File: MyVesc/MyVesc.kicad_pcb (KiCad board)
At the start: 4 copper layers, 100 x 70 mm, 112 parts, among them J1 CAN, J10 GATE_PH_A, J11 CURR_SENS_PH_A, J12 CURR_SENS_PH_B, J13 CURR_SENS_PH_C, J14 Pull_up, J2 Conn_01x08, J4 Conn_01x03, J5 UNUSED MCU PINS, J6 TEMP_SENS, J7 V_IN, J8 GATE_PH_C, J9 GATE_PH_B, P4 HALL/Encoder, P5 SWD, U1 TJA1051T/3/1J, U10 LM5161, U11 MCP16311/2, U12 MCP16311/2, U13 INA240, U14 INA240, U15 INA240, U2 BMI160, U3 STM32F405RGT6, U4 UCC2721x, U5 UCC2721x, U6 UCC2721x, Y1 8M

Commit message: routerd logic board
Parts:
- removed C61, C62: 2.2u, Capacitor_SMD:C_0603_1608Metric
- removed J10: GATE_PH_A, Connector_PinHeader_1.00mm:PinHeader_1x06_P1.00mm_Vertical
- removed J11: CURR_SENS_PH_A, Connector_PinHeader_1.00mm:PinHeader_1x04_P1.00mm_Vertical
- removed J12: CURR_SENS_PH_B, Connector_PinHeader_1.00mm:PinHeader_1x04_P1.00mm_Vertical
- removed J13: CURR_SENS_PH_C, Connector_PinHeader_1.00mm:PinHeader_1x04_P1.00mm_Vertical
- removed J9: GATE_PH_B, Connector_PinHeader_1.00mm:PinHeader_1x06_P1.00mm_Vertical
- removed R1: 22R, Resistor_SMD:R_0603_1608Metric
- removed U13, U14, U15: INA240, Package_SO:SOIC-8_3.9x4.9mm_P1.27mm
- added C24: 2.2u, Capacitor_SMD:C_0603_1608Metric, F.Cu at (234.1, 123.8)
- added C25: 2.2u, Capacitor_SMD:C_0603_1608Metric, F.Cu at (243.0, 148.8)
- added C26: 2.2u, Capacitor_SMD:C_0603_1608Metric, F.Cu at (277.9, 145.7)
- added C48: 2.2u, Capacitor_SMD:C_0603_1608Metric, F.Cu at (263.4, 150.5)
- added C49: 2.2u, Capacitor_SMD:C_0603_1608Metric, F.Cu at (286.6, 147.2)
- added J15: PH_C_CONNECTOR, Connector_PinSocket_2.54mm:PinSocket_2x04_P2.54mm_Vertical, B.Cu at (297.3, 151.3)
- added J3: PH_A_CONNECTOR, Connector_PinSocket_2.54mm:PinSocket_2x04_P2.54mm_Vertical, B.Cu at (207.9, 151.6)
- added R30: 10k, Resistor_SMD:R_0603_1608Metric, F.Cu at (235.2, 122.7)
- added R31: 10k, Resistor_SMD:R_0603_1608Metric, F.Cu at (241.4, 148.8)
- added R32: 10k, Resistor_SMD:R_0603_1608Metric, F.Cu at (276.3, 145.7)
- added U7: INA210, Package_TO_SOT_SMD:SOT-363_SC-70-6, F.Cu at (215.6, 150.5)
- added U8: INA210, Package_TO_SOT_SMD:SOT-363_SC-70-6, F.Cu at (260.9, 150.5)
- added U9: INA210, Package_TO_SOT_SMD:SOT-363_SC-70-6, F.Cu at (286.6, 149.7)
- C13, R16, R17, R18, R2, R20, R21, R22, R3, R4, R5, R6: moved to F.Cu
- J6: value TEMP_SENS -> PH_B_CONNECTOR; footprint Connector_PinHeader_1.00mm:PinHeader_1x08_P1.00mm_Vertical -> Connector_PinSocket_2.54mm:PinSocket_2x04_P2.54mm_Vertical; moved to B.Cu
- J7: footprint Connector_PinHeader_1.00mm:PinHeader_1x02_P1.00mm_Vertical -> Connector_PinSocket_2.54mm:PinSocket_1x02_P2.54mm_Vertical; moved to B.Cu
- J8: value GATE_PH_C -> NRF bluetooth; footprint Connector_PinHeader_1.00mm:PinHeader_1x06_P1.00mm_Vertical -> Connector_JST:JST_PH_B4B-PH-K_1x04_P2.00mm_Vertical
- USB1: footprint Connector_USB:USB_Micro-B_Wuerth_614105150721_Vertical -> Connector_USB:USB_Mini-B_Lumberg_2486_01_Horizontal
- moved J4 281.9 mm to (282.4, 89.0), turned to 180 degrees
- moved C1 276.7 mm to (282.4, 93.2), turned to -90 degrees
- moved R10 270.3 mm to (278.4, 93.2), turned to 90 degrees
- moved P4 260.0 mm to (297.6, 97.4), turned to -90 degrees
- moved J14 253.7 mm to (292.1, 107.0)
- moved R4 251.9 mm to (294.5, 104.2), turned to 90 degrees
- moved R5 251.7 mm to (292.9, 104.2), turned to 90 degrees
- moved R6 251.7 mm to (291.4, 104.2), turned to 90 degrees
- moved J6 239.9 mm to (252.8, 151.6)
- moved R2 216.2 mm to (290.8, 118.5), turned to 0 degrees
- moved USB1 214.3 mm to (297.4, 118.7), turned to 90 degrees
- moved R3 213.9 mm to (290.8, 120.0), turned to 0 degrees
- moved J8 213.8 mm to (297.5, 92.2), turned to 90 degrees
- moved C63 206.1 mm to (223.1, 149.2), turned to 180 degrees
- moved C27 204.4 mm to (224.6, 101.2)
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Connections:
- J5 pad 1: PB2 -> unconnected-(J5-Pin_1-Pad1)
- J5 pad 2: PB12 -> unconnected-(J5-Pin_2-Pad2)
- J5 pad 4: PC13 -> PB12
- J5 pad 6: PC14 -> PC13
- J5 pad 8: PA15 -> PC14
- J6 pad 1: VCC -> /Power MOSFETS/PH_B_IN+
- J6 pad 2: GND -> /Power MOSFETS/PH_B_IN-
- J6 pad 3: /MCU/ADC_TEMP3 -> GND
- J6 pad 4: GND -> /Power MOSFETS/TEMP2
- J6 pad 5: /MCU/ADC_TEMP2 -> /Mosfet driver/LO2
- J6 pad 6: GND -> VCC
- J6 pad 7: /MCU/ADC_TEMP -> /Mosfet driver/HS2
- J6 pad 8: GND -> /Mosfet driver/HO2
- J8 pad 1: /Mosfet driver/HO3 -> GND
- J8 pad 2: GND -> /MCU/PC11_UART_RX
- J8 pad 3: /Mosfet driver/HS3 -> /MCU/PC10_UART_TX
- J8 pad 4: GND -> +5V
- U3 pad 17: /MCU/ADC_TEMP -> /Power MOSFETS/TEMP
- U3 pad 26: /MCU/ADC_TEMP2 -> /Power MOSFETS/TEMP2
- U3 pad 27: /MCU/ADC_TEMP3 -> /Power MOSFETS/TEMP3
- USB1 pad 1: Net-(USB1-VBUS) -> +5V
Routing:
- net VCC: track 92.7 -> 467.8 mm, vias 2 -> 27
- net +5V: track 35.7 -> 208.6 mm, vias 2 -> 10
- net +12V: track 129.5 -> 296.2 mm, vias 4 -> 9
- net /Power MOSFETS/TEMP3: track 0.00 -> 95.7 mm, vias 0 -> 3
- net PB12: track 0.00 -> 71.5 mm, vias 0 -> 5
- net PC13: track 0.00 -> 65.6 mm, vias 0 -> 1
- net /Power MOSFETS/TEMP: track 0.00 -> 65.3 mm
- net /MCU/HALL_1: track 0.00 -> 64.5 mm
- net /MCU/TEMP_MOTOR: track 0.00 -> 63.9 mm
- net PC14: track 0.00 -> 63.8 mm, vias 0 -> 1
- net /MCU/PC10_UART_TX: track 0.00 -> 61.4 mm
- net /MCU/VOLTAGE_3: track 3.82 -> 64.7 mm, vias 1 -> 2
- net /MCU/HALL_2: track 0.00 -> 60.5 mm, vias 0 -> 3
- net /MCU/HALL_3: track 0.00 -> 57.2 mm, vias 0 -> 2
- net /MCU/PC11_UART_RX: track 0.00 -> 57.1 mm
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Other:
- board size 100 x 70 mm -> 100 x 73.7 mm

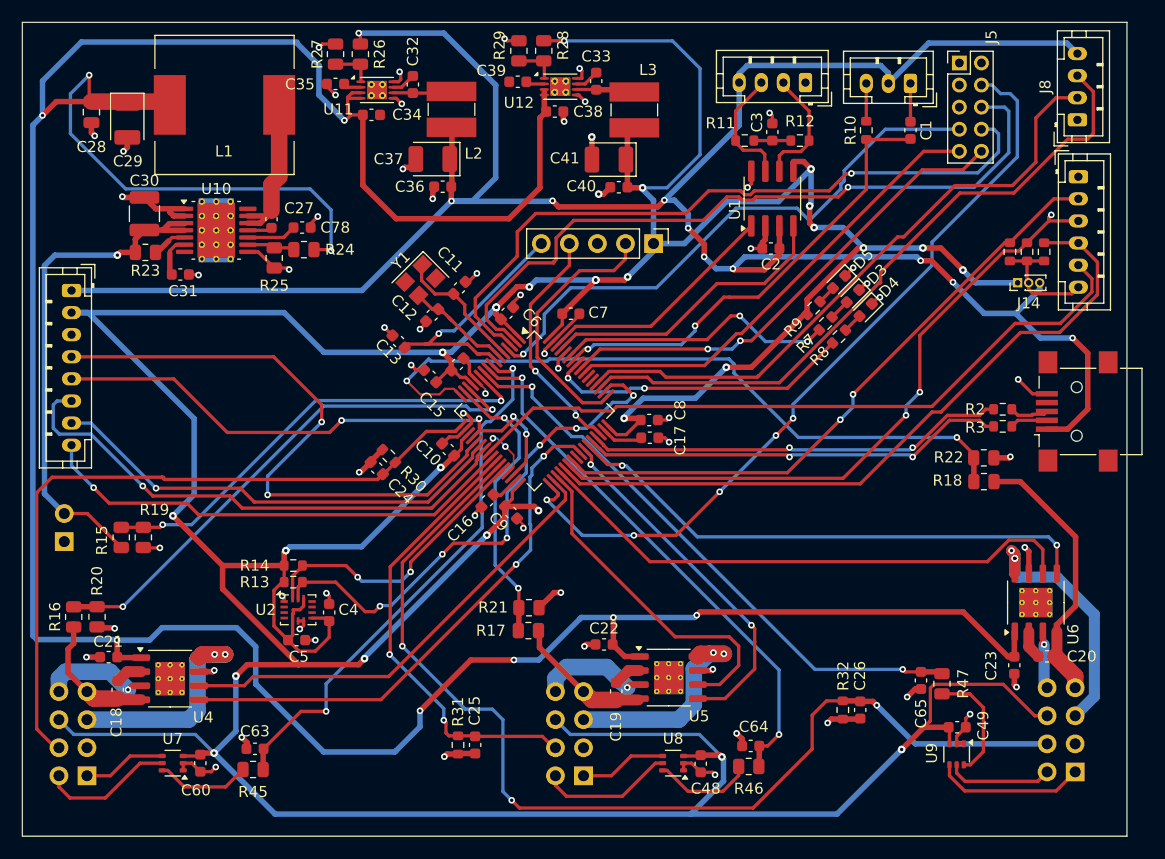
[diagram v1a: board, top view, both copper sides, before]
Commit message: moved curr amps
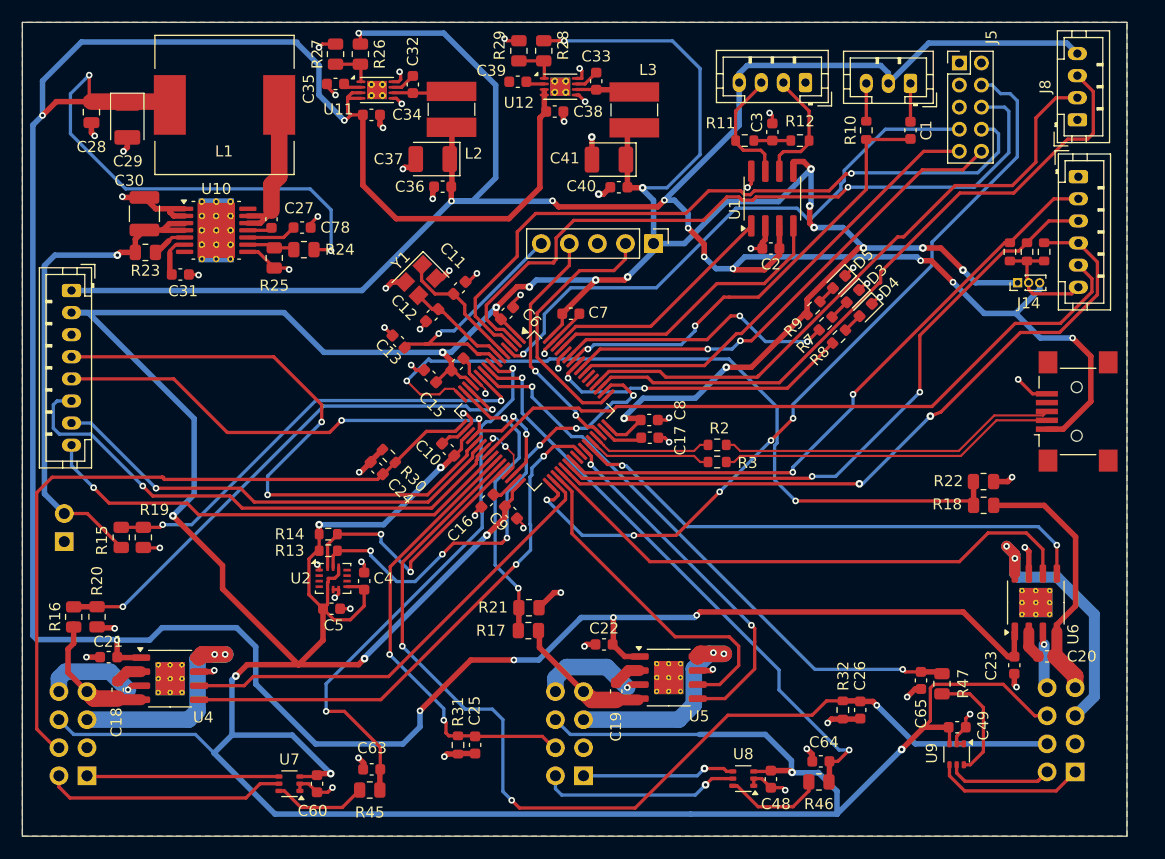
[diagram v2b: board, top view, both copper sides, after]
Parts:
- moved R2 26.1 mm to (264.9, 121.7)
- moved R3 26.1 mm to (264.9, 123.2)
- moved C63 10.7 mm to (233.6, 151.1)
- moved C60 10.7 mm to (228.7, 152.3)
- moved U7 10.7 mm to (226.2, 152.3)
- moved R45 10.7 mm to (233.4, 152.9)
- moved C48 6.50 mm to (269.8, 151.9)
- moved R46 6.50 mm to (274.1, 152.2)
- moved C64 6.50 mm to (274.3, 150.3)
- moved U8 6.50 mm to (267.3, 151.9)
- moved C5 4.26 mm to (230.0, 136.5)
- moved C4 4.26 mm to (232.9, 134.0)
- moved R13 4.26 mm to (229.7, 131.3)
- moved R14 4.26 mm to (229.7, 129.8)
- moved U2 4.26 mm to (230.1, 133.8)
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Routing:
- net /USB_+: track 3.61 -> 31.2 mm
- net /MCU/USB_D-: track 38.7 -> 11.2 mm, vias 2 -> 0
- net /MCU/USB_D+: track 38.1 -> 10.9 mm, vias 2 -> 0
- net /USB_-: track 3.40 -> 30.6 mm
- net VCC: track 467.8 -> 478.8 mm, vias 27 -> 24
- net /Power MOSFETS/PH_A_IN+: track 7.81 -> 17.7 mm
- net /Power MOSFETS/PH_A_IN-: track 12.1 -> 21.9 mm
- net /Power MOSFETS/PH_B_IN+: track 7.90 -> 13.9 mm, vias 0 -> 1
- net /Power MOSFETS/PH_B_IN-: track 12.2 -> 18.1 mm, vias 0 -> 1
- net /MCU/VOLTAGE_3: track 64.7 -> 70.0 mm
- net GND: track 119.7 -> 124.8 mm, vias 61 -> 64
- net /MCU/CURRENT_2: track 49.6 -> 54.2 mm
- net PA15: track 47.4 -> 43.4 mm
- net PB2: track 26.9 -> 24.7 mm
- net +12V: track 296.2 -> 294.1 mm
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- added copper zone on B.Cu, net GND
- added copper zone on F.Cu, net GND

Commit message: ongoing
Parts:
- moved J4 1.30 mm to (282.4, 87.7)
- moved J1 1.22 mm to (272.9, 87.7)
- moved J8 0.94 mm to (298.4, 92.2)
- moved P4 0.90 mm to (298.5, 97.4)
- moved J2 0.45 mm to (206.0, 107.7)
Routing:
- net /MCU/HALL_1: track 64.5 -> 69.4 mm
- net /MCU/TEMP_MOTOR: track 63.9 -> 65.4 mm
- net +5V: track 208.6 -> 209.9 mm
- net Net-(J4-Pin_3): track 3.42 -> 4.72 mm
- net GND: track 124.8 -> 126.1 mm
- net /CAN bus transceiver/CANL: track 10.8 -> 12.0 mm
- net /CAN bus transceiver/CANH: track 11.0 -> 12.1 mm
- net /MCU/PC11_UART_RX: track 57.1 -> 58.0 mm
- net /MCU/HALL_3: track 57.4 -> 58.3 mm
- net /MCU/HALL_2: track 59.3 -> 60.2 mm
- net /MCU/PC10_UART_TX: track 61.4 -> 62.0 mm

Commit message: final
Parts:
- J7: moved to F.Cu
- R15, R16, R17, R18: value 68k -> 150k
- R19: value 2.2k -> 4k7
- R20, R21, R22: value 2k2 -> 4k7
- moved C38 0.83 mm to (249.4, 91.6)
- moved J7 0.06 mm to (205.8, 130.4), turned to 180 degrees
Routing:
- net +5V: track 209.9 -> 222.1 mm
- net +12V: track 294.1 -> 297.9 mm
- net VCC: track 478.8 -> 482.0 mm
- net Net-(U12-BOOST): track 2.22 -> 3.64 mm
- net Net-(U12-VCC): track 1.71 -> 3.03 mm
- net GND: track 126.1 -> 125.2 mm, vias 64 -> 220
- net Net-(U11-SW): track 6.12 -> 5.58 mm
